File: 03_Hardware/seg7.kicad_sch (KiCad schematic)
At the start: 40 parts, among them U201 KCSA02-106, U202 74HC595, U203 KCSA02-106, U204 74HC595, U205 KCSA02-106, U206 74HC595, U207 KCSA02-106, U208 74HC595

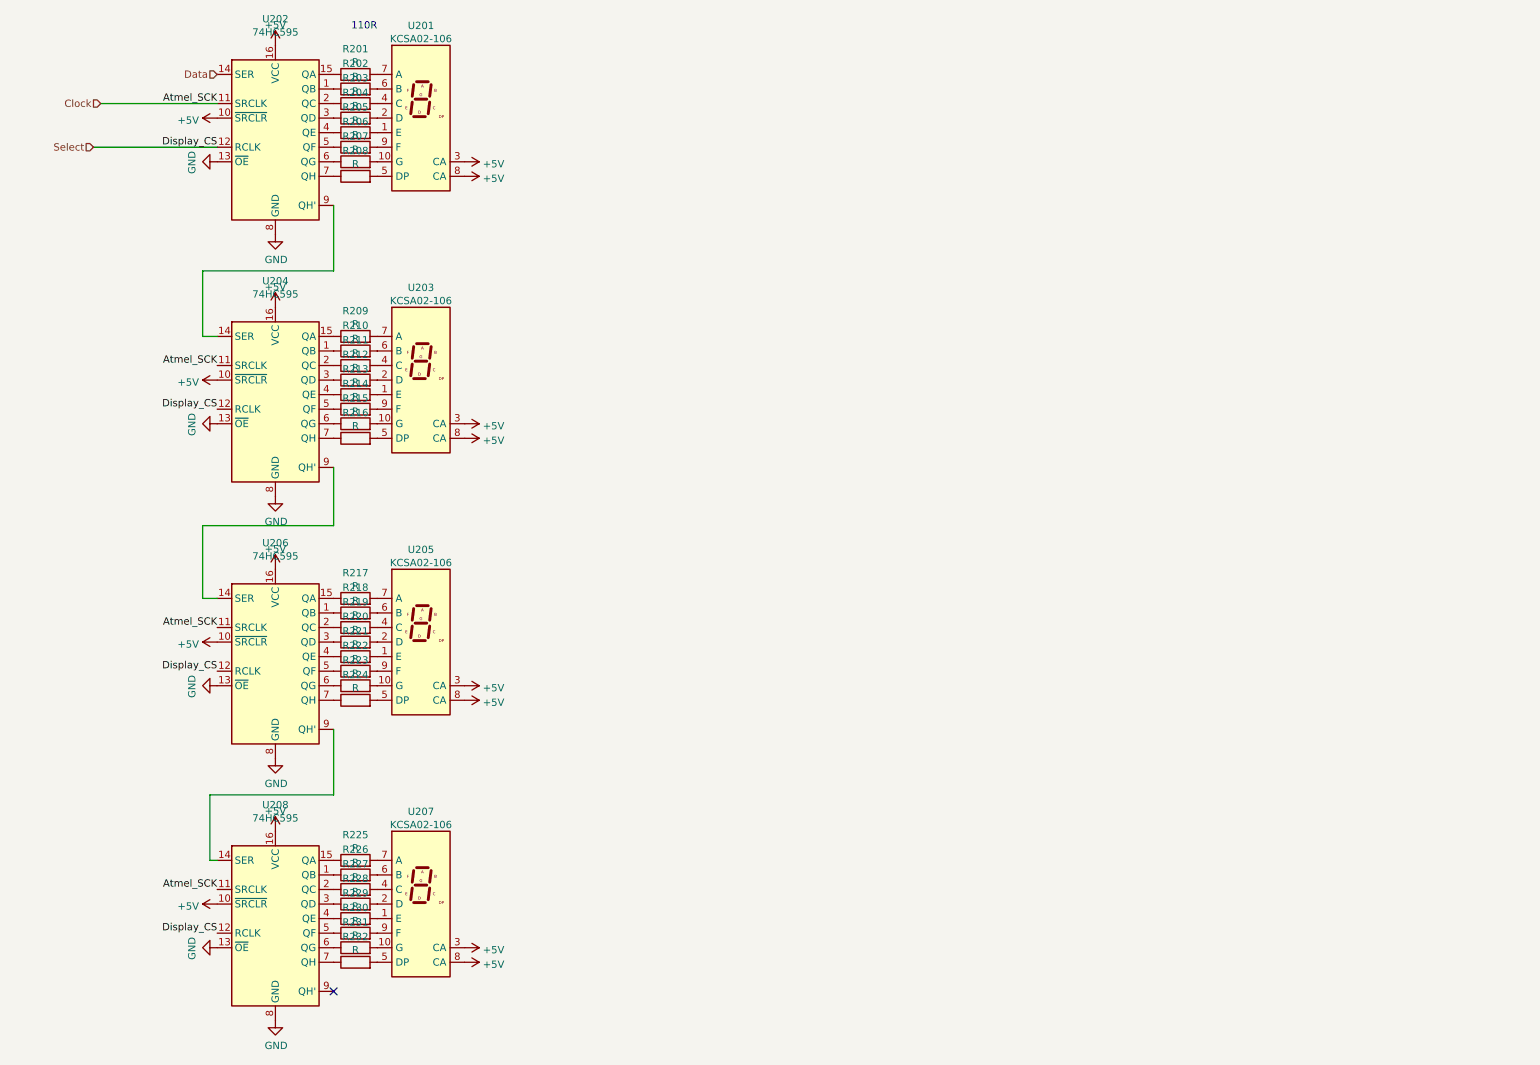
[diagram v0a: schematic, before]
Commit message: Anzeigeplan weiter, Datenblatt der 0,56" Anzeige dazugefügt
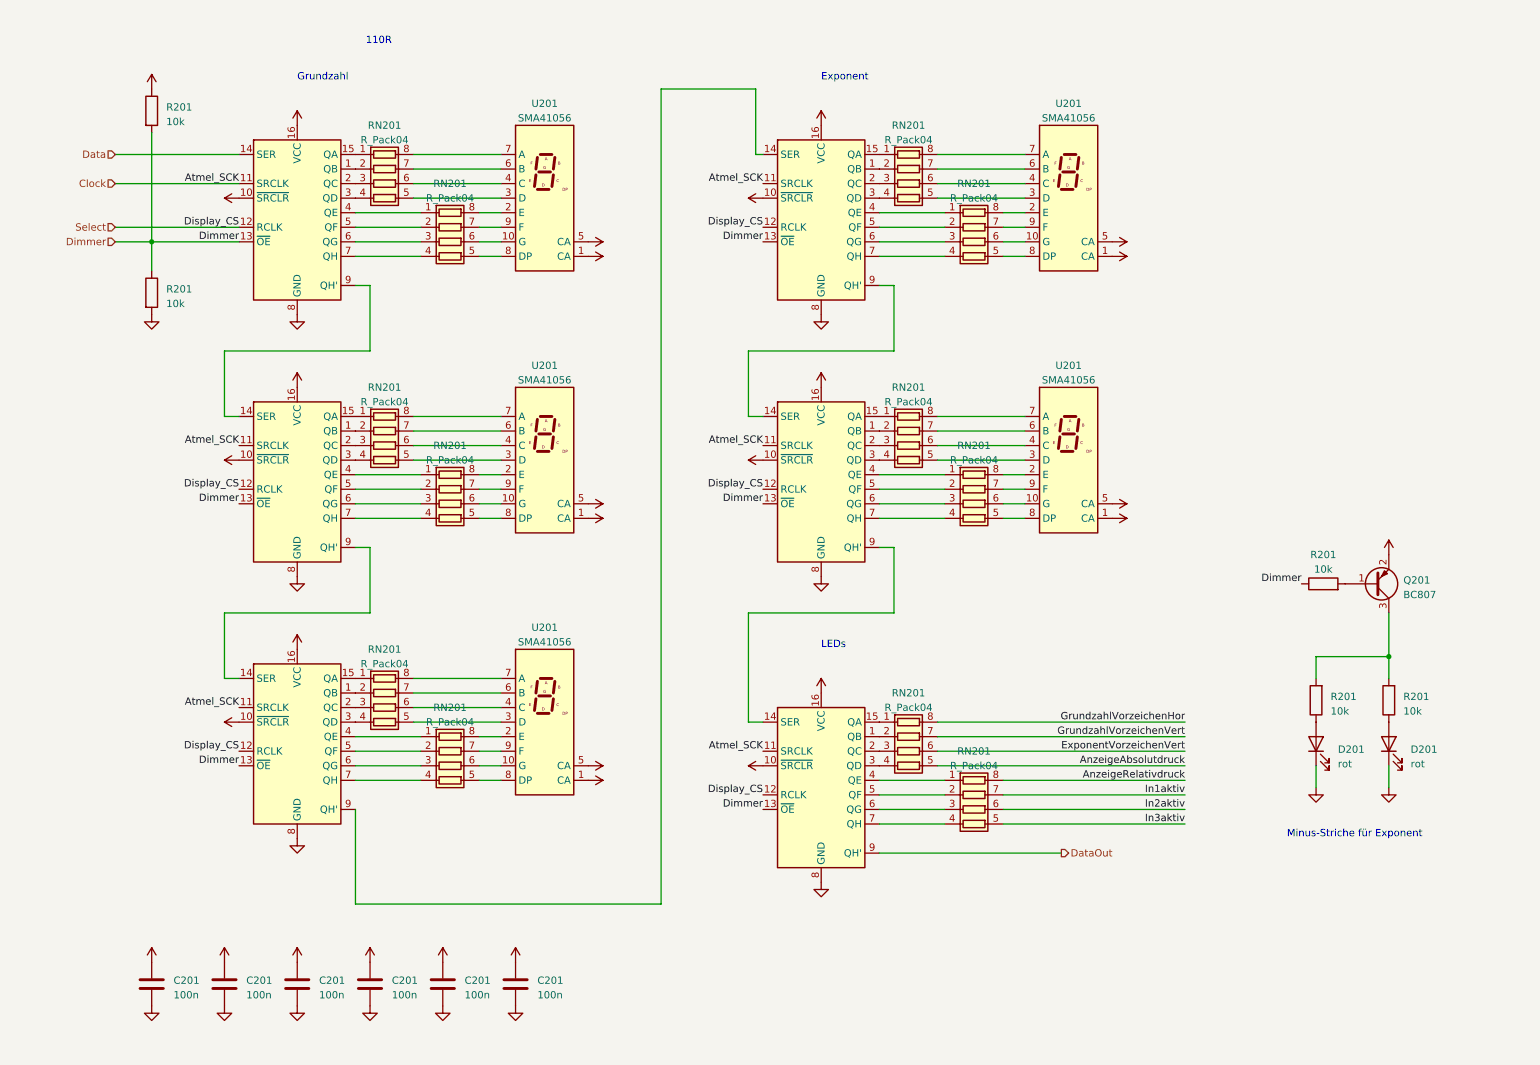
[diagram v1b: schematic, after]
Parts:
- removed R201, R202, R203, R204, R205, R206, R207, R208, R209, R210, R211, R212, R213, R214, R215, R216, R217, R218, R219, R220, R221, R222, R223, R224, R225, R226, R227, R228, R229, R230, R231, R232: R, Resistor_SMD:R_0805_2012Metric, symbol Device:R
- removed U201, U203, U205, U207: KCSA02-106, Display_7Segment:7SEGMENT-LED__HDSM531_HDSM533_SMD, symbol Display_Character:KCSA02-106
- added ? (x2): (no value), symbol 74xx:74HC595
- added C201 (x6): 100n, Resistor_SMD:R_0603_1608Metric, symbol Device:C
- added D201 (x2): rot, symbol Device:LED
- added Q201: BC807, Package_TO_SOT_SMD:SOT-23, symbol Transistor_BJT:BC807
- added R201 (x5): 10k, symbol Device:R
- added RN201 (x12): R_Pack04, symbol Device:R_Pack04
- added U201 (x5): SMA41056, Display_7Segment:SA15-11xxx, symbol Display_Character:SA15-11EWA
- ?: renamed from U208; value 74HC595 -> (none); footprint Package_SO:SOIC-16_3.9x9.9mm_P1.27mm -> (none)
- ?: renamed from U204; value 74HC595 -> (none); footprint Package_SO:SOIC-16_3.9x9.9mm_P1.27mm -> (none)
- ?: renamed from U202; value 74HC595 -> (none); footprint Package_SO:SOIC-16_3.9x9.9mm_P1.27mm -> (none)
- ?: renamed from U206; value 74HC595 -> (none); footprint Package_SO:SOIC-16_3.9x9.9mm_P1.27mm -> (none)
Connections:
- net +5V: now also ?.10 (~{SRCLR}), ?.10 (~{SRCLR}), ?.16 (VCC), ?.16 (VCC), C201.1, C201.1, C201.1, C201.1, C201.1, C201.1, Q201.2 (E), R201.1, U201.1 (CA), U201.1 (CA), U201.1 (CA), U201.1 (CA), U201.1 (CA), U201.5 (CA), U201.5 (CA), U201.5 (CA), U201.5 (CA), U201.5 (CA)
- net Clock: now also ?.11 (SRCLK), ?.11 (SRCLK)
- net GND: now also ?.8 (GND), ?.8 (GND), C201.2, C201.2, C201.2, C201.2, C201.2, C201.2, D201.1 (K), D201.1 (K), R201.2; no longer ?.13 (~{OE}), ?.13 (~{OE}), ?.13 (~{OE}), ?.13 (~{OE})
- net Select: now also ?.12 (RCLK), ?.12 (RCLK)
- net at ?.6 (QG): now also RN201.3 (R3.1) (x4)
- net at ?.1 (QB): now also RN201.2 (R2.1) (x4)
- net at ?.15 (QA): now also RN201.1 (R1.1) (x4)
- net at ?.2 (QC): now also RN201.3 (R3.1) (x4)
- net at ?.3 (QD): now also RN201.4 (R4.1) (x4)
- net at ?.4 (QE): now also RN201.1 (R1.1) (x4)
- net at ?.5 (QF): now also RN201.2 (R2.1) (x4)
- net at ?.7 (QH): now also RN201.4 (R4.1) (x4)
- net at ?.9 (QH'): now also ?.14 (SER)
- new net: RN201.6 (R3.2), U201.10 (G) (x5)
- new net: RN201.8 (R1.2), U201.2 (E) (x5)
- new net: RN201.5 (R4.2), U201.3 (D) (x5)
- new net: RN201.6 (R3.2), U201.4 (C) (x5)
- new net: RN201.7 (R2.2), U201.6 (B) (x5)
- new net: RN201.8 (R1.2), U201.7 (A) (x5)
- new net: RN201.5 (R4.2), U201.8 (DP) (x5)
- new net: RN201.7 (R2.2), U201.9 (F) (x5)
- new net: ?.4 (QE), RN201.1 (R1.1) (x2)
- new net: ?.5 (QF), RN201.2 (R2.1) (x2)
- new net: ?.6 (QG), RN201.3 (R3.1) (x2)
- new net: ?.7 (QH), RN201.4 (R4.1) (x2)
- new net: ?.1 (QB), RN201.2 (R2.1) (x2)
- new net: ?.15 (QA), RN201.1 (R1.1) (x2)
- new net: ?.2 (QC), RN201.3 (R3.1) (x2)
- new net: ?.3 (QD), RN201.4 (R4.1) (x2)
- new net: ?.14 (SER), ?.9 (QH')
- new net: D201.2 (A), R201.1 (x2)
- new net: Q201.3 (C), R201.2, R201.2
- new net: Q201.1 (B), R201.2
- new net AnzeigeAbsolutdruck: RN201.5 (R4.2)
- new net AnzeigeRelativdruck: RN201.8 (R1.2)
- new net DataOut: ?.9 (QH')
- new net Dimmer: ?.13 (~{OE}), ?.13 (~{OE}), ?.13 (~{OE}), ?.13 (~{OE}), ?.13 (~{OE}), ?.13 (~{OE}), R201.1, R201.1, R201.2
- new net ExponentVorzeichenVert: RN201.6 (R3.2)
- new net GrundzahlVorzeichenHor: RN201.8 (R1.2)
- new net GrundzahlVorzeichenVert: RN201.7 (R2.2)
- new net In1aktiv: RN201.7 (R2.2)
- new net In2aktiv: RN201.6 (R3.2)
- new net In3aktiv: RN201.5 (R4.2)
- no-connect marks 1 -> 0
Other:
- note added: "Exponent"
- note added: "Grundzahl"
- note added: "LEDs"
- note added: "Minus-Striche für Exponent"
- company: (none) -> Institut für theoretischen Igorismus
- title: (none) -> LED-Anzeigen und Einzelleds, dimmbar

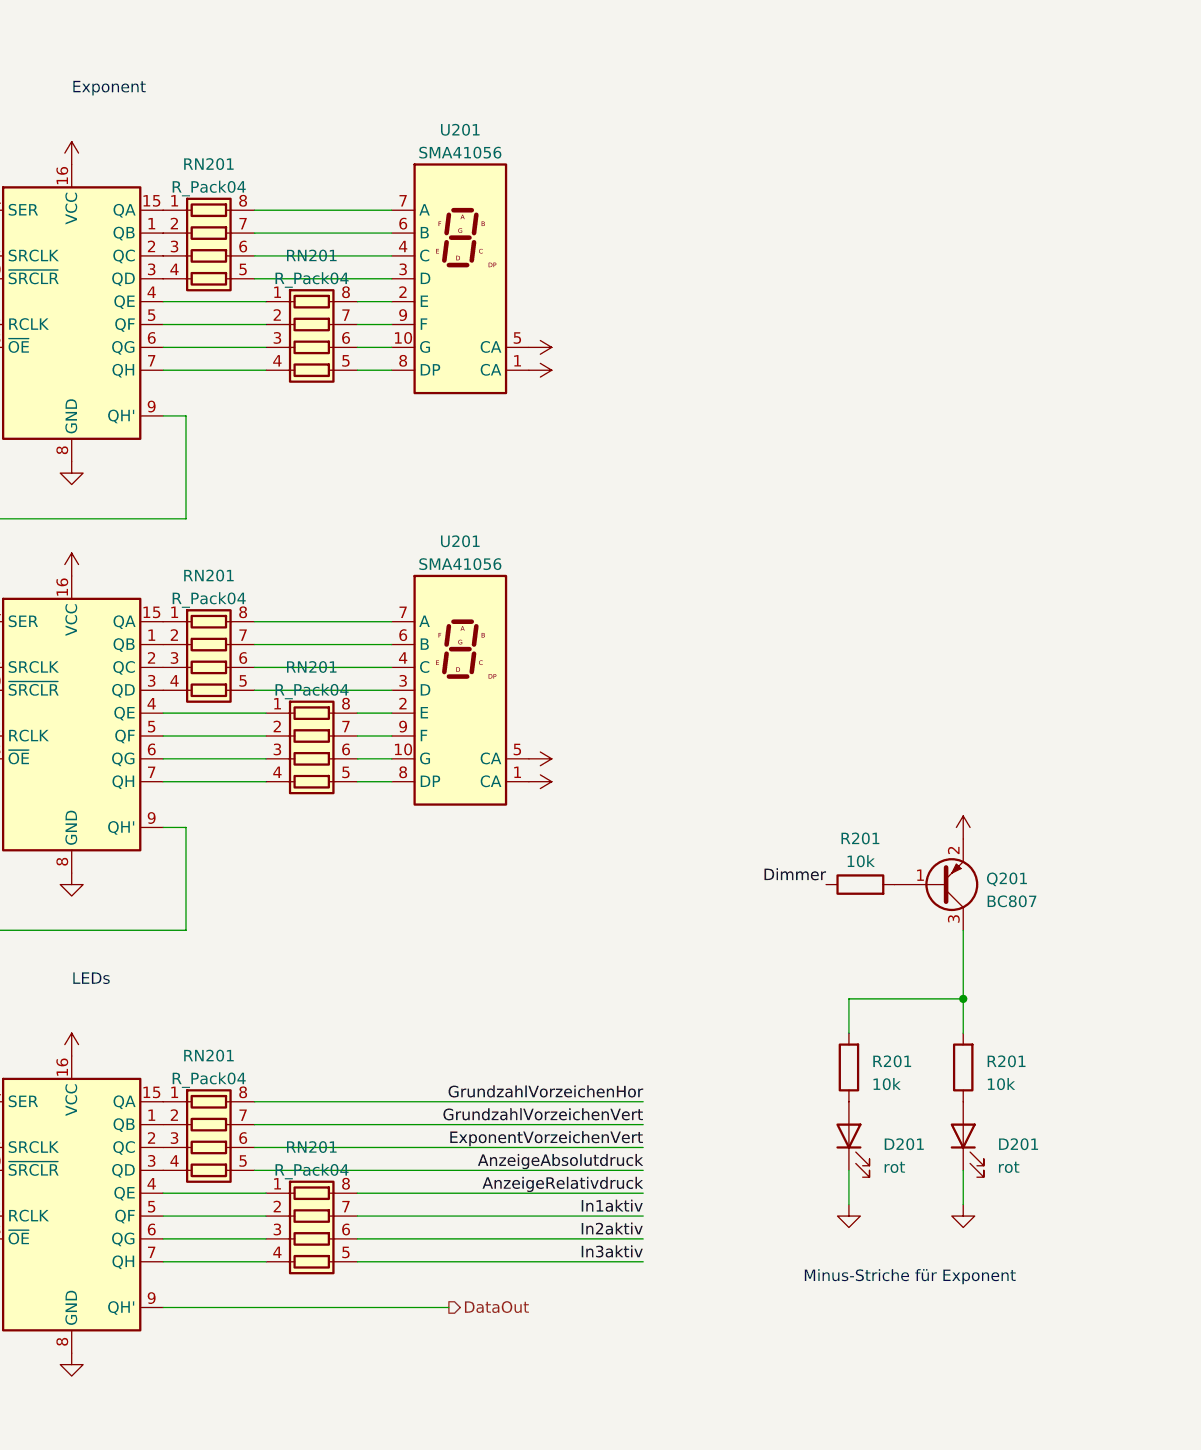
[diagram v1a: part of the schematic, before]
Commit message: Schaltplan Main erweitert und PSU/Ausgänge hinzugefügt
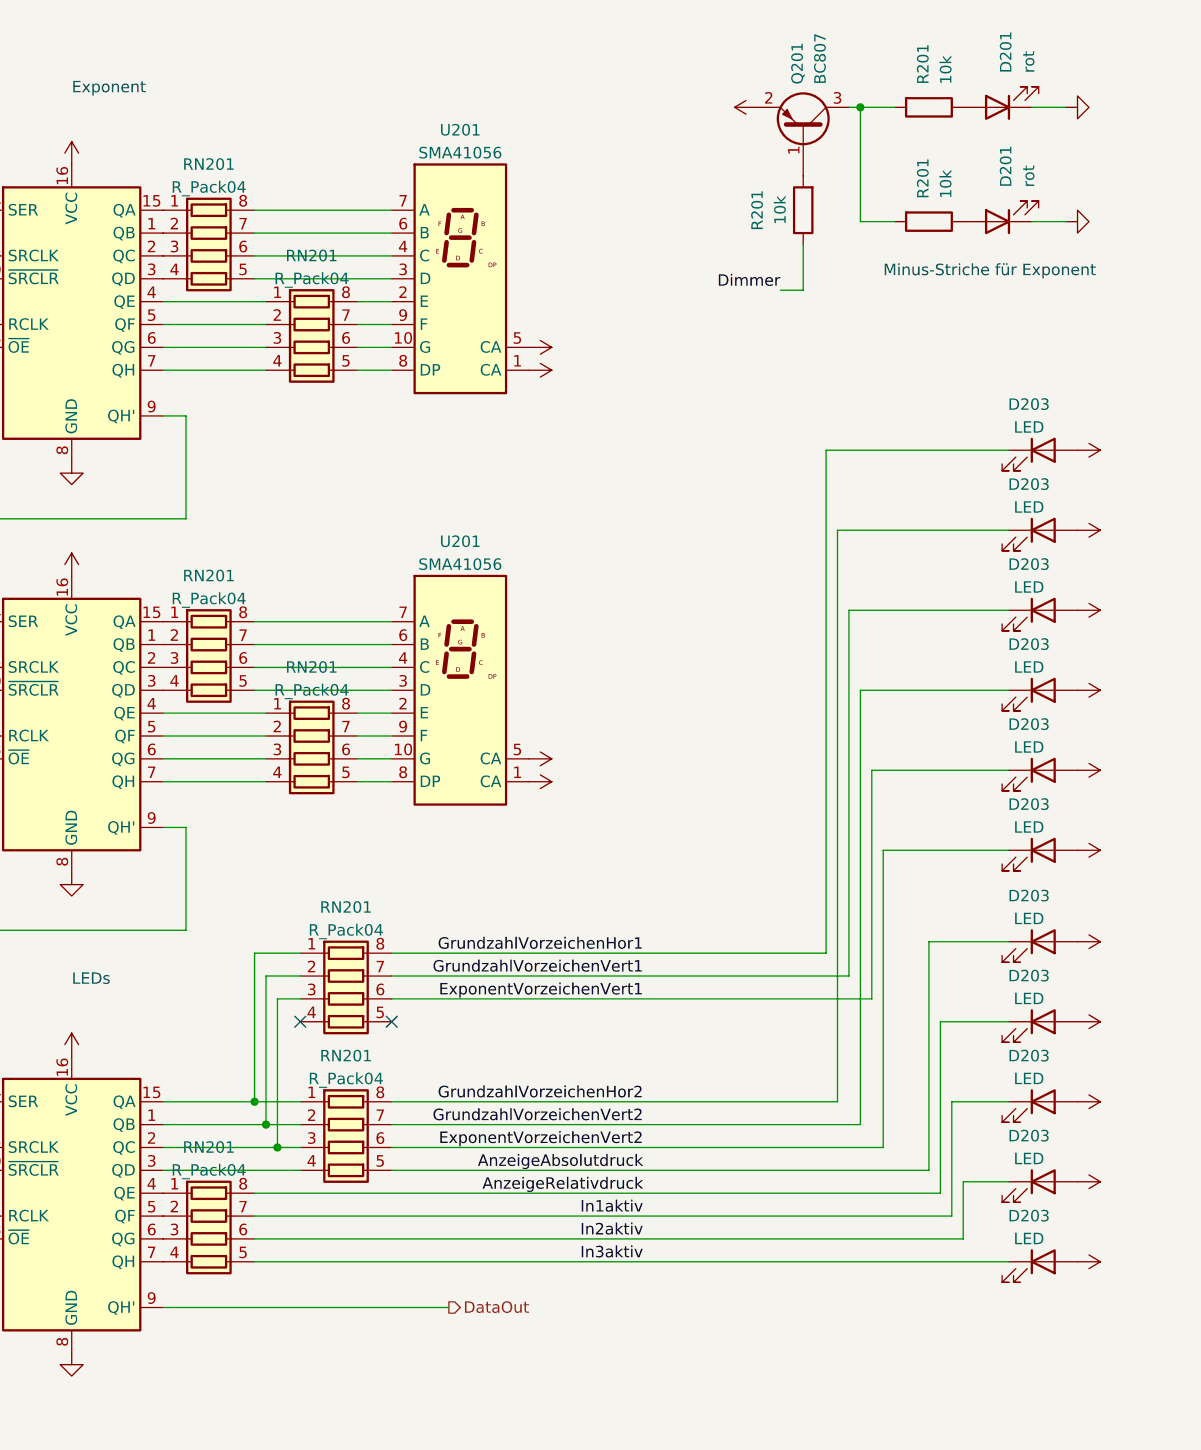
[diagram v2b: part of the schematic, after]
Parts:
- added D203 (x11): LED, symbol Device:LED
- added RN201: R_Pack04, symbol Device:R_Pack04
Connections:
- net +5V: now also D203.2 (A), D203.2 (A), D203.2 (A), D203.2 (A), D203.2 (A), D203.2 (A), D203.2 (A), D203.2 (A), D203.2 (A), D203.2 (A), D203.2 (A)
- net AnzeigeAbsolutdruck: now also D203.1 (K)
- net AnzeigeRelativdruck: now also D203.1 (K)
- net In1aktiv: now also D203.1 (K)
- net In2aktiv: now also D203.1 (K)
- net In3aktiv: now also D203.1 (K)
- net at ?.1 (QB), RN201.2 (R2.1): now also RN201.2 (R2.1)
- net at ?.15 (QA), RN201.1 (R1.1): now also RN201.1 (R1.1)
- net at ?.2 (QC), RN201.3 (R3.1): now also RN201.3 (R3.1)
- net ExponentVorzeichenVert renamed ExponentVorzeichenVert2
- net ExponentVorzeichenVert2: now also D203.1 (K)
- net GrundzahlVorzeichenHor renamed GrundzahlVorzeichenHor2
- net GrundzahlVorzeichenHor2: now also D203.1 (K)
- net GrundzahlVorzeichenVert renamed GrundzahlVorzeichenVert2
- net GrundzahlVorzeichenVert2: now also D203.1 (K)
- new net ExponentVorzeichenVert1: D203.1 (K), RN201.6 (R3.2)
- new net GrundzahlVorzeichenHor1: D203.1 (K), RN201.8 (R1.2)
- new net GrundzahlVorzeichenVert1: D203.1 (K), RN201.7 (R2.2)
- no-connect marks 0 -> 2
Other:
- moved on the sheet: D201, Q201, R201, RN201
